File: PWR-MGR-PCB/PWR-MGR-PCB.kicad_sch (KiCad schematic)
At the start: 0 parts

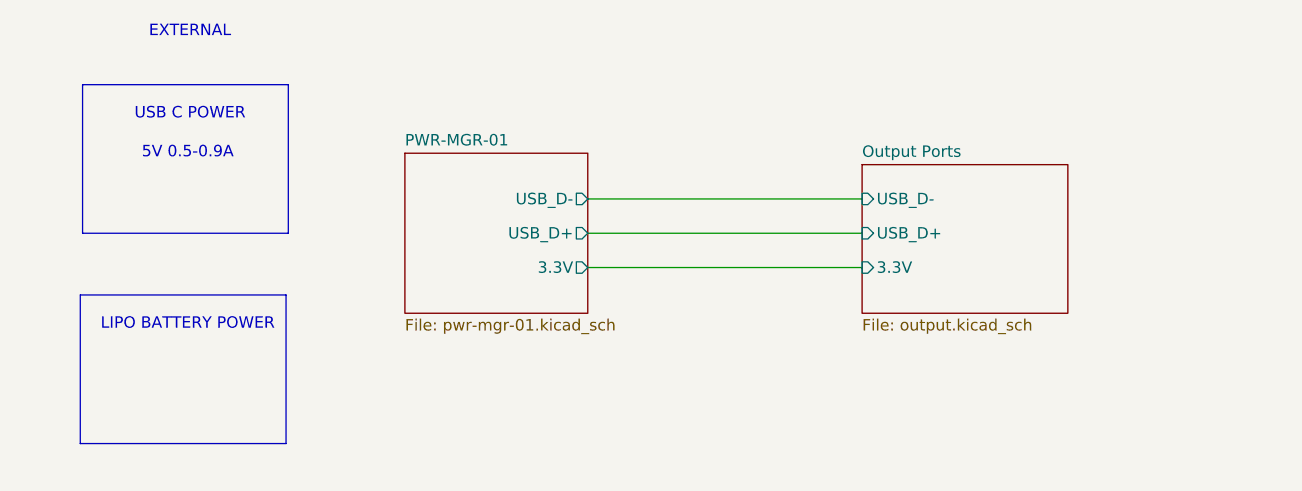
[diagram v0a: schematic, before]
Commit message: Update layout, optimize sub-sheet for reusability
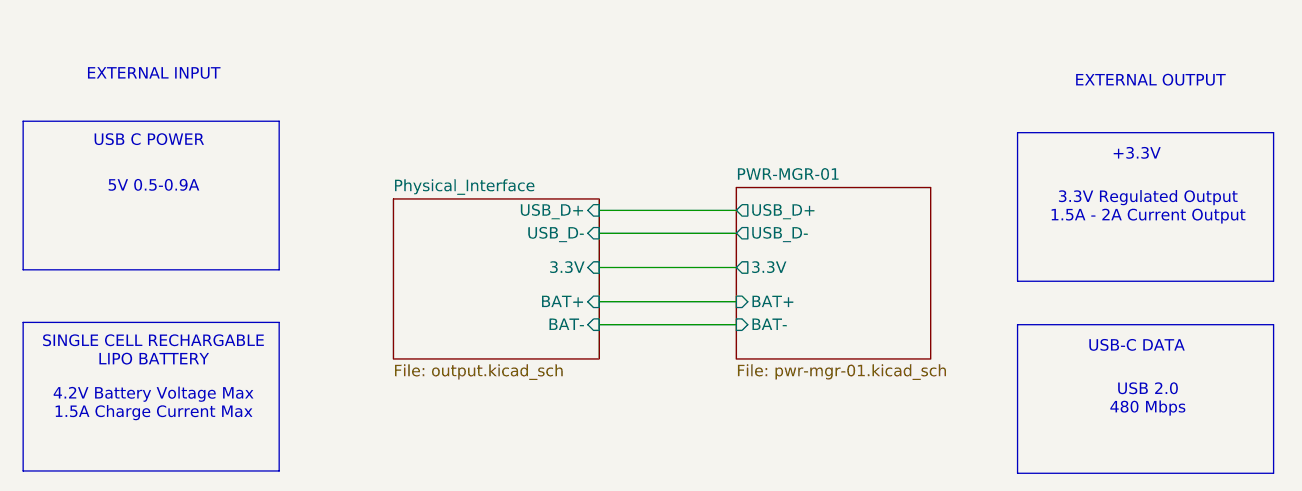
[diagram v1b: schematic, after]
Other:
- sheet Output Ports renamed Physical_Interface
- sheet PWR-MGR-01 ports: added BAT+, BAT-; removed none
- sheet Physical_Interface ports: added BAT+, BAT-; removed none
- note added: "+3.3V"
- note added: "3.3V Regulated Output 1.5A - 2A Current Output"
- note added: "4.2V Battery Voltage Max 1.5A Charge Current Max"
- note added: "EXTERNAL INPUT"
- note added: "EXTERNAL OUTPUT"
- note added: "SINGLE CELL RECHARGABLE LIPO BATTERY"
- note added: "USB 2.0 480 Mbps"
- note added: "USB-C DATA"
- note removed: "EXTERNAL"
- note removed: "LIPO BATTERY POWER"
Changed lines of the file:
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@@
 	)
 	(rectangle
-		(start 91.186 73.66)
-		(end 114.046 90.17)
+		(start 84.582 77.724)
+		(end 113.03 94.234)
 		(stroke
 			(width 0)
@@
 	)
 	(rectangle
-		(start 90.932 97.028)
-		(end 113.792 113.538)
+		(start 195.072 100.33)
+		(end 223.52 116.84)
 		(stroke
 			(width 0)
@@
 		)
 	)
-	(text "LIPO BATTERY POWER"
-		(exclude_from_sim no)
-		(at 102.87 100.33 0)
-		(effects
-			(font
-				(size 1.27 1.27)
-			)
-		)
-	)
-	(text "EXTERNAL"
-		(exclude_from_sim no)
-		(at 103.124 67.818 0)
+	(rectangle
+		(start 195.072 78.994)
+		(end 223.52 95.504)
+		(stroke
+			(width 0)
+			(type default)
+		)
+		(fill
+			(type none)
+		)
+	)
+	(rectangle
+		(start 84.582 100.076)
+		(end 113.03 116.586)
+		(stroke
+			(width 0)
+			(type default)
+		)
+		(fill
+			(type none)
+		)
+	)
+	(text "SINGLE CELL RECHARGABLE \nLIPO BATTERY"
+		(exclude_from_sim no)
+		(at 99.06 103.378 0)
+		(effects
+			(font
+				(size 1.27 1.27)
+			)
+		)
+	)
+	(text "USB 2.0\n480 Mbps"
+		(exclude_from_sim no)
+		(at 209.55 108.712 0)
+		(effects
+			(font
+				(size 1.27 1.27)
+			)
+		)
+	)
+	(text "3.3V Regulated Output\n1.5A - 2A Current Output"
+		(exclude_from_sim no)
+		(at 209.55 87.376 0)
 		(effects
 			(font
@@
 	(text "5V 0.5-0.9A\n"
 		(exclude_from_sim no)
-		(at 102.87 81.28 0)
+		(at 99.06 85.09 0)
+		(effects
+			(font
+				(size 1.27 1.27)
+			)
+		)
+	)
+	(text "EXTERNAL INPUT"
+		(exclude_from_sim no)
+		(at 99.06 72.644 0)
+		(effects
+			(font
+				(size 1.27 1.27)
+			)
+		)
+	)
+	(text "4.2V Battery Voltage Max\n1.5A Charge Current Max"
+		(exclude_from_sim no)
+		(at 99.06 109.22 0)
+		(effects
+			(font
+				(size 1.27 1.27)
+			)
+		)
+	)
+	(text "USB-C DATA"
+		(exclude_from_sim no)
+		(at 208.28 102.87 0)
+		(effects
+			(font
+				(size 1.27 1.27)
+			)
+		)
+	)
+	(text "EXTERNAL OUTPUT"
+		(exclude_from_sim no)
+		(at 209.804 73.406 0)
 		(effects
 			(font
@@
 	(text "USB C POWER\n"
 		(exclude_from_sim no)
-		(at 103.124 76.962 0)
-		(effects
-			(font
-				(size 1.27 1.27)
-			)
-		)
-	)
-	(wire
-		(pts
-			(xy 147.32 86.36) (xy 177.8 86.36)
-		)
-		(stroke
-			(width 0)
-			(type default)
-		)
-	)
-	(wire
-		(pts
-			(xy 147.32 93.98) (xy 177.8 93.98)
-		)
-		(stroke
-			(width 0)
-			(type default)
-		)
-	)
-	(wire
-		(pts
-			(xy 147.32 90.17) (xy 177.8 90.17)
+		(at 98.552 80.01 0)
+		(effects
+			(font
+				(size 1.27 1.27)
+			)
+		)
+	)
+	(text "+3.3V"
+		(exclude_from_sim no)
+		(at 208.28 81.534 0)
+		(effects
+			(font
+				(size 1.27 1.27)
+			)
+		)
+	)
+	(wire
+		(pts
+			(xy 148.59 100.33) (xy 163.83 100.33)
+		)
+		(stroke
+			(width 0)
+			(type default)
+		)
+	)
+	(wire
+		(pts
+			(xy 148.59 90.17) (xy 163.83 90.17)
+		)
+		(stroke
+			(width 0)
+			(type default)
+		)
+	)
+	(wire
+		(pts
+			(xy 148.59 97.79) (xy 163.83 97.79)
+		)
+		(stroke
+			(width 0)
+			(type default)
+		)
+	)
+	(wire
+		(pts
+			(xy 148.59 87.63) (xy 163.83 87.63)
+		)
+		(stroke
+			(width 0)
+			(type default)
+		)
+	)
+	(wire
+		(pts
+			(xy 148.59 93.98) (xy 163.83 93.98)
 		)
 		(stroke
@@
 	)
 	(sheet
-		(at 177.8 82.55)
-		(size 22.86 16.51)
+		(at 125.73 86.36)
+		(size 22.86 17.78)
 		(exclude_from_sim no)
 		(in_bom yes)
@@
 			(color 0 0 0 0.0000)
 		)
-		(property "Sheetname" "Output Ports"
-			(at 177.8 81.8384 0)
+		(property "Sheetname" "Physical_Interface"
+			(at 125.73 85.6484 0)
 			(effects
 				(font
@@
 		)
 		(property "Sheetfile" "output.kicad_sch"
-			(at 177.8 99.6446 0)
+			(at 125.73 104.7246 0)
 			(effects
 				(font
@@
 		)
 		(pin "3.3V" input
-			(at 177.8 93.98 180)
-			(effects
-				(font
-					(size 1.27 1.27)
-				)
-				(justify left)
+			(at 148.59 93.98 0)
+			(effects
+				(font
+					(size 1.27 1.27)
+				)
+				(justify right)
 			)
 		)
 		(pin "USB_D+" input
-			(at 177.8 90.17 180)
-			(effects
-				(font
-					(size 1.27 1.27)
-				)
-				(justify left)
+			(at 148.59 87.63 0)
+			(effects
+				(font
+					(size 1.27 1.27)
+				)
+				(justify right)
 			)
 		)
 		(pin "USB_D-" input
-			(at 177.8 86.36 180)
-			(effects
-				(font
-					(size 1.27 1.27)
-				)
-				(justify left)
+			(at 148.59 90.17 0)
+			(effects
+				(font
+					(size 1.27 1.27)
+				)
+				(justify right)
+			)
+		)
+		(pin "BAT-" input
+			(at 148.59 100.33 0)
+			(effects
+				(font
+					(size 1.27 1.27)
+				)
+				(justify right)
+			)
+		)
+		(pin "BAT+" input
+			(at 148.59 97.79 0)
+			(effects
+				(font
+					(size 1.27 1.27)
+				)
+				(justify right)
 			)
 		)
@@
 	)
 	(sheet
-		(at 127 81.28)
-		(size 20.32 17.78)
+		(at 163.83 85.09)
+		(size 21.59 19.05)
 		(exclude_from_sim no)
 		(in_bom yes)
@@
 		)
 		(property "Sheetname" "PWR-MGR-01"
-			(at 127 80.5684 0)
+			(at 163.83 84.3784 0)
 			(effects
 				(font
@@
 		)
 		(property "Sheetfile" "pwr-mgr-01.kicad_sch"
-			(at 127 99.6446 0)
+			(at 163.83 104.7246 0)
 			(effects
 				(font
@@
 		)
 		(pin "USB_D+" output
-			(at 147.32 90.17 0)
-			(effects
-				(font
-					(size 1.27 1.27)
-				)
-				(justify right)
+			(at 163.83 87.63 180)
+			(effects
+				(font
+					(size 1.27 1.27)
+				)
+				(justify left)
 			)
 		)
 		(pin "3.3V" output
-			(at 147.32 93.98 0)
-			(effects
-				(font
-					(size 1.27 1.27)
-				)
-				(justify right)
+			(at 163.83 93.98 180)
+			(effects
+				(font
+					(size 1.27 1.27)
+				)
+				(justify left)
 			)
 		)
 		(pin "USB_D-" output
-			(at 147.32 86.36 0)
-			(effects
-				(font
-					(size 1.27 1.27)
-				)
-				(justify right)
-			)
-		)
+			(at 163.83 90.17 180)
+			(effects
+				(font
+					(size 1.27 1.27)
+				)
+				(justify left)
+			)
+		)
+		(pin "BAT-" input
+			(at 163.83 100.33 180)
+			(effects
+				(font
+					(size 1.27 1.27)
+				)
+				(justify left)
+			)
+		)
+		(pin "BAT+" input
+			(at 163.83 97.79 180)
+			(effects
+				(font
+					(size 1.27 1.27)
+				)
+				(justify left)
+			)
+		)
